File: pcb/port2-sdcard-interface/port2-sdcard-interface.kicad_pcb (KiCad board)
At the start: 4 copper layers, 85.1 x 100 mm, 65 parts, among them J1 Micro_SD_Card_Det1, J2 P2000T Port 2, U1 CY62128ELL-45SXI, U10 74HC32, U11 74HC273, U12 74HC165, U13 74HC595, U14 74HC00, U15 SST39SF010, U16 AMS1117-3.3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

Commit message: Fixing value in schematic
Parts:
- C23: value 100nF -> 100uF

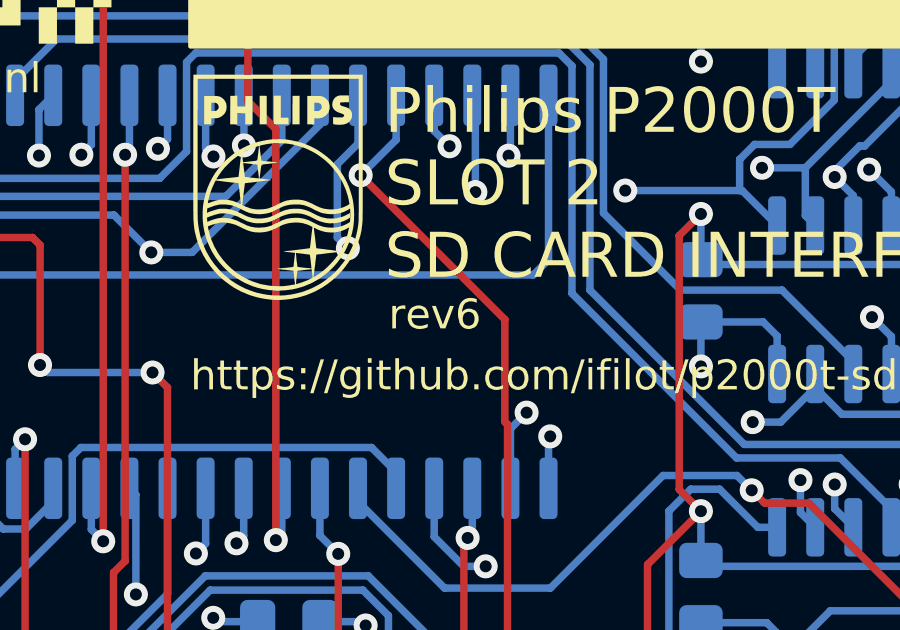
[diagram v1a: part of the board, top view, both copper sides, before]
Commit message: Removing copper pour around edge connector (#17)
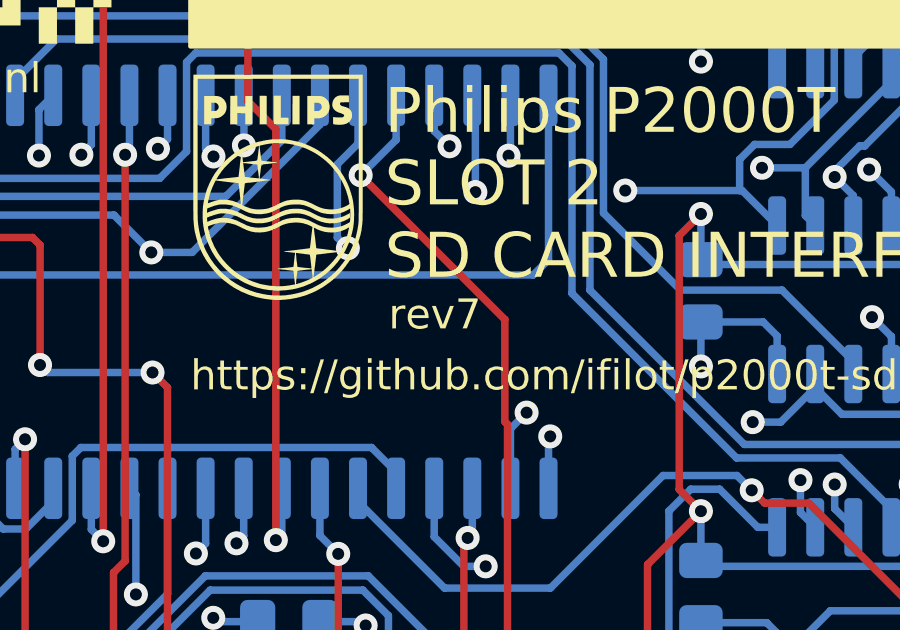
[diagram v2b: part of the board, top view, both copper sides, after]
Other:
- board text added: "rev7"
- board text removed: "rev6"
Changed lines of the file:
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@@
 		)
 	)
-	(gr_text "rev6"
+	(gr_text "rev7"
 		(at 66.021 64.883 0)
 		(layer "F.SilkS")
@@
 		(polygon
 			(pts
-				(xy 21.571 102.348) (xy 101.708 102.475) (xy 101.708 117.969) (xy 21.317 118.096)
+				(xy 21.571 102.348) (xy 101.708 102.475) (xy 101.708 117.715) (xy 21.571 117.969)
 			)
 		)
@@
 		(polygon
 			(pts
-				(xy 21.571 17.766) (xy 110.405 17.766) (xy 101.581 117.969) (xy 21.317 117.969)
+				(xy 21.571 17.766) (xy 110.405 17.766) (xy 101.581 107.809) (xy 21.571 107.809)
 			)
 		)
@@
 		(polygon
 			(pts
-				(xy 21.571 17.766) (xy 110.405 17.73) (xy 101.581 117.969) (xy 21.317 117.969)
+				(xy 21.571 17.766) (xy 110.405 17.73) (xy 101.581 107.809) (xy 21.571 107.809)
 			)
 		)
